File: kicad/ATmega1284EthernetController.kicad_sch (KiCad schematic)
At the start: 43 parts, among them J1 AVR-ISP-6, J2 PA0-7, J3 PC0-7, J4 PB0-3/PD3-7, J5 Barrel_Jack_MountingPin, J6 SIO, J7 RJ45_Amphenol_RJMG1BD3B8K1ANR, SW1 RESET, U1 ATmega1284P-A, U2 74HCT32, U3 ENC28J60x-SP, U4 LM7805_TO220, Y1 20MHz, Y2 25MHz

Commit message: Changed footprint of AVR-ISP
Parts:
- J1: footprint Connector_PinHeader_1.00mm:PinHeader_2x03_P1.00mm_Vertical -> Connector_PinHeader_2.54mm:PinHeader_2x03_P2.54mm_Vertical

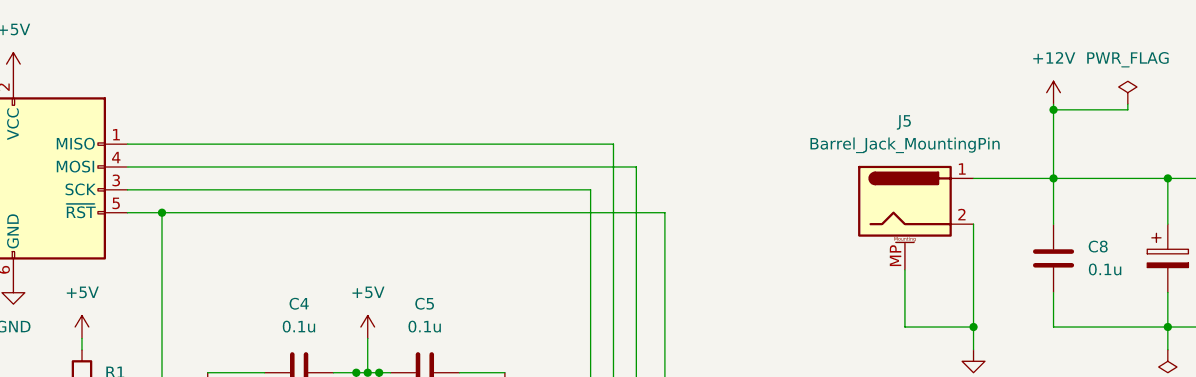
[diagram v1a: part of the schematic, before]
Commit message: Update ATmega1284EthernetController.kicad_sch
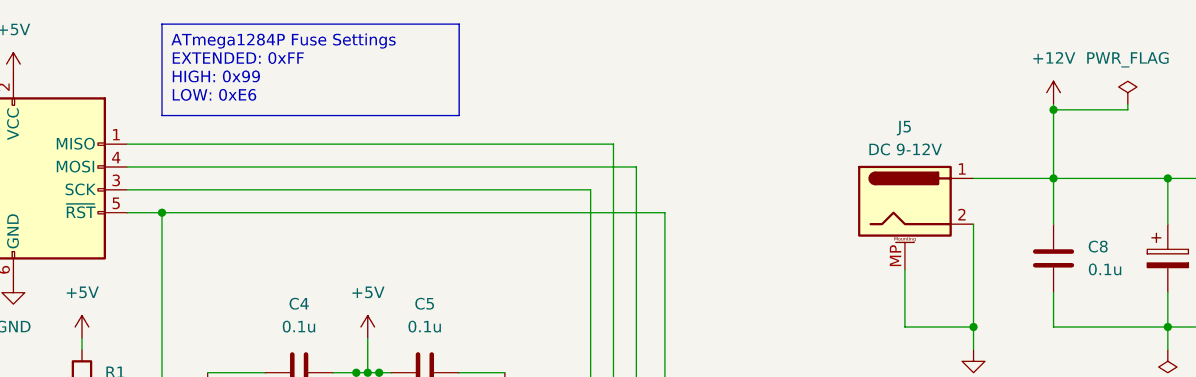
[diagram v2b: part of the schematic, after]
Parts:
- J5: value Barrel_Jack_MountingPin -> DC 9-12V
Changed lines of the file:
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@@
     (stroke (width 0) (type default))
+  )
+  (text_box "ATmega1284P Fuse Settings\nEXTENDED: 0xFF\nHIGH: 0x99\nLOW: 0xE6"
+    (at 46.99 15.24 0) (size 33.02 10.16)
+    (stroke (width 0) (type default))
+    (fill (type none))
+    (effects (font (size 1.27 1.27)) (justify left top))
   )
   (label "PB0" (at 98.425 180.975 90) (fields_autoplaced)
@@
   (symbol (lib_id "Connector:Barrel_Jack_MountingPin") (at 129.54 34.925 0) (unit 1)
     (in_bom yes) (on_board yes) (dnp no) (fields_autoplaced)
-    (property "Reference" "J5" (at 129.54 26.035 0)
-      (effects (font (size 1.27 1.27)))
-    )
-    (property "Value" "Barrel_Jack_MountingPin" (at 129.54 28.575 0)
-      (effects (font (size 1.27 1.27)))
-    )
+    (property "Reference" "J5" (at 129.54 26.67 0)
+      (effects (font (size 1.27 1.27)))
+    )
+    (property "Value" "DC 9-12V" (at 129.54 29.21 0)
+      (effects (font (size 1.27 1.27)))
+    )

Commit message: PCB base
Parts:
- removed J5: DC 9-12V, Connector_BarrelJack:BarrelJack_Horizontal, symbol Connector:Barrel_Jack_MountingPin
- removed J6: SIO, Connector_PinHeader_2.54mm:PinHeader_1x04_P2.54mm_Vertical, symbol Connector:Conn_01x04_Pin
- removed U4: LM7805_TO220, Package_TO_SOT_THT:TO-220-3_Vertical, symbol Regulator_Linear:LM7805_TO220
- added J1: DC2 9-12V, Connector_PinHeader_2.00mm:PinHeader_1x04_P2.00mm_Vertical, symbol Connector:Conn_01x04_Pin
- added J3: DC1 9-12V, Connector_BarrelJack:BarrelJack_Horizontal, symbol Connector:Barrel_Jack
- added J8: SIO, Connector_PinHeader_2.54mm:PinHeader_1x04_P2.54mm_Vertical, symbol Connector:Conn_01x04_Pin
- added SW1: SELECT, Button_Switch_THT:SW_Slide_1P2T_CK_OS102011MS2Q, symbol Switch:SW_SPDT
- added U2: LM7805, Package_TO_SOT_THT:TO-220-3_Vertical, symbol Regulator_Linear:LM7805_TO220
- renumbered C15 to C1, C7 to C10, C2 to C11, C3 to C15, C8 to C2, C9 to C3, C11 to C4, C4 to C5, C5 to C6, C10 to C7, C1 to C8, C6 to C9, J1 to J2, J7 to J4, J2 to J5, J3 to J6, J4 to J7, R11 to R10, R5 to R11, R6 to R2, R8 to R3, R2 to R4, R3 to R5, R4 to R6, R9 to R8, R10 to R9, SW1 to SW2, U2 to U1, U1 to U4
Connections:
- net +5V: now also C1.2, C11.2, J5.10 (Pin_10), J6.10 (Pin_10), J8.4 (Pin_4), U2.3 (VO); no longer C1.1, C11.1, J5.9 (Pin_9), J6.9 (Pin_9)
- net GND: now also C1.1, C10.1, C11.1, C9.1, J5.9 (Pin_9), J6.9 (Pin_9), R11.1, J1.3 (Pin_3), J1.4 (Pin_4), J3.2, J8.3 (Pin_3), U2.2 (GND); no longer C1.2, C10.2, C11.2, C9.2, J5.10 (Pin_10), J6.10 (Pin_10), R11.2
- net RX0: now also J8.1 (Pin_1)
- net TX0: now also J8.2 (Pin_2)
- net at U3.14 (RBIAS): now also R11.2; no longer R11.1
- net at U3.23 (OSC1), Y2.1: now also C9.2; no longer C9.1
- net at U3.24 (OSC2), Y2.2: now also C10.2; no longer C10.1
- net +12V: no longer names the net of C2.1, C3.1
- net +12V: now also SW1.2 (B), U2.1 (VI)
- new net: J1.1 (Pin_1), J1.2 (Pin_2), SW1.1 (A)
- new net: J3.1, SW1.3 (C)
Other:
- moved on the sheet: C1, C10, C11, C12, C13, C14, C15, C2, C3, C4, C5, C6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
